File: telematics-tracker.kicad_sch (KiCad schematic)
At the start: 0 parts

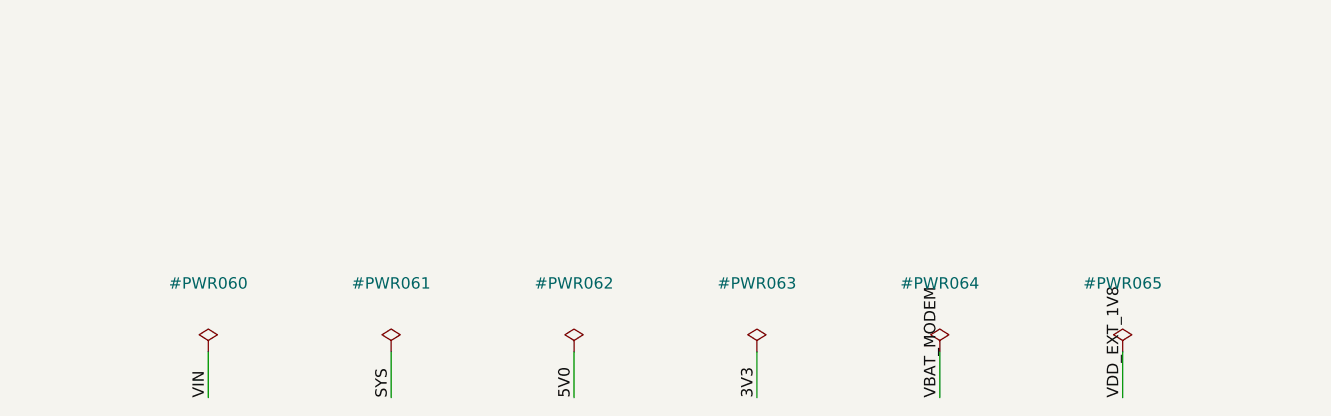
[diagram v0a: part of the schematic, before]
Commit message: M2: io re-committed ERC-clean with F-10 + F-11 applied
F-10: two-stage non-inverting NPN gate driver (2x MMBT3904 C20526 + 4.7k/
10k/10k/2.2k per channel) from 5V0; gate swing ~4.1V where AM2390N RDS is
specified. Default-OFF proven structurally by the netlist guard (8/8
assertions: gate pulldown, MCU-side base pulldown, QnB base pullup, QnB
collector on driver node, both channels). Consequence logged: DO1/DO2
inactive during battery backup. handoff section 6 note updated per
instruction.
F-11: SS310 -> SS3200 C65001 (200V 3A SMA), both channels.
ERC 0 errors; section-5 checklist 48/48 with far ends updated.
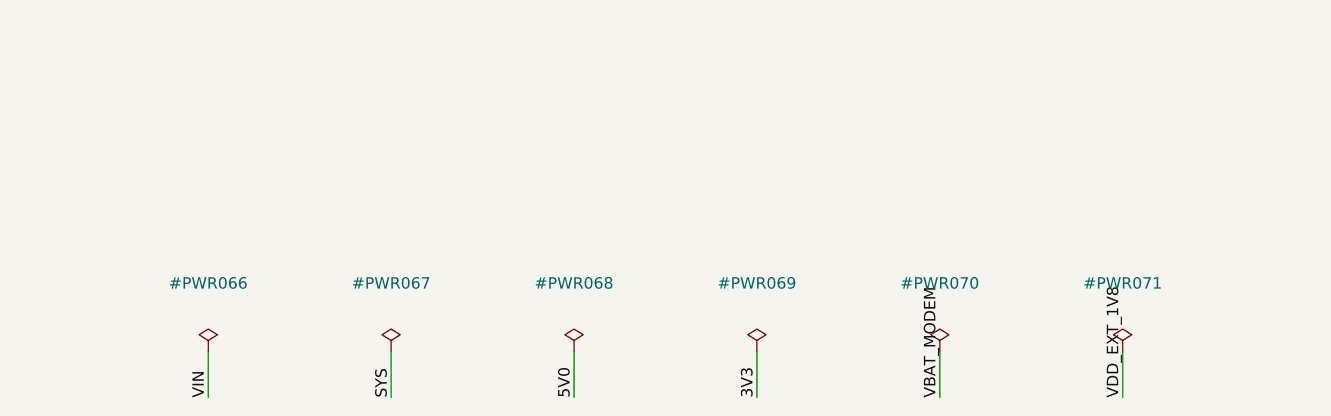
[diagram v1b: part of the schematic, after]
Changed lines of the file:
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@@
 		(dnp no)
 		(fields_autoplaced yes)
-		(property "Reference" "#PWR060"
+		(property "Reference" "#PWR066"
 			(at 25.4 261.62 0)
 			(effects
@@
 			(project "telematics-tracker"
 				(path "/784bc421-9fc7-43cb-bfc3-562714cb3f68"
-					(reference "#PWR060")
+					(reference "#PWR066")
 					(unit 1)
 				)
@@
 		(dnp no)
 		(fields_autoplaced yes)
-		(property "Reference" "#PWR061"
+		(property "Reference" "#PWR067"
 			(at 45.72 261.62 0)
 			(effects
@@
 			(project "telematics-tracker"
 				(path "/784bc421-9fc7-43cb-bfc3-562714cb3f68"
-					(reference "#PWR061")
+					(reference "#PWR067")
 					(unit 1)
 				)
@@
 		(dnp no)
 		(fields_autoplaced yes)
-		(property "Reference" "#PWR062"
+		(property "Reference" "#PWR068"
 			(at 66.04 261.62 0)
 			(effects
@@
 			(project "telematics-tracker"
 				(path "/784bc421-9fc7-43cb-bfc3-562714cb3f68"
-					(reference "#PWR062")
+					(reference "#PWR068")
 					(unit 1)
 				)
@@
 		(dnp no)
 		(fields_autoplaced yes)
-		(property "Reference" "#PWR063"
+		(property "Reference" "#PWR069"
 			(at 86.36 261.62 0)
 			(effects
@@
 			(project "telematics-tracker"
 				(path "/784bc421-9fc7-43cb-bfc3-562714cb3f68"
-					(reference "#PWR063")
+					(reference "#PWR069")
 					(unit 1)
 				)
@@
 		(dnp no)
 		(fields_autoplaced yes)
-		(property "Reference" "#PWR064"
+		(property "Reference" "#PWR070"
 			(at 106.68 261.62 0)
 			(effects
@@
 			(project "telematics-tracker"
 				(path "/784bc421-9fc7-43cb-bfc3-562714cb3f68"
-					(reference "#PWR064")
+					(reference "#PWR070")
 					(unit 1)
 				)
@@
 		(dnp no)
 		(fields_autoplaced yes)
-		(property "Reference" "#PWR065"
+		(property "Reference" "#PWR071"
 			(at 127 261.62 0)
 			(effects
@@
 			(project "telematics-tracker"
 				(path "/784bc421-9fc7-43cb-bfc3-562714cb3f68"
-					(reference "#PWR065")
-					(unit 1)
-				)
+					(reference "#PWR071")
+					(unit 1)
+				)
